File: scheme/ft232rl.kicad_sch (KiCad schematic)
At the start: 10 parts, among them J3 USB_B_Mini, U3 FT232RL

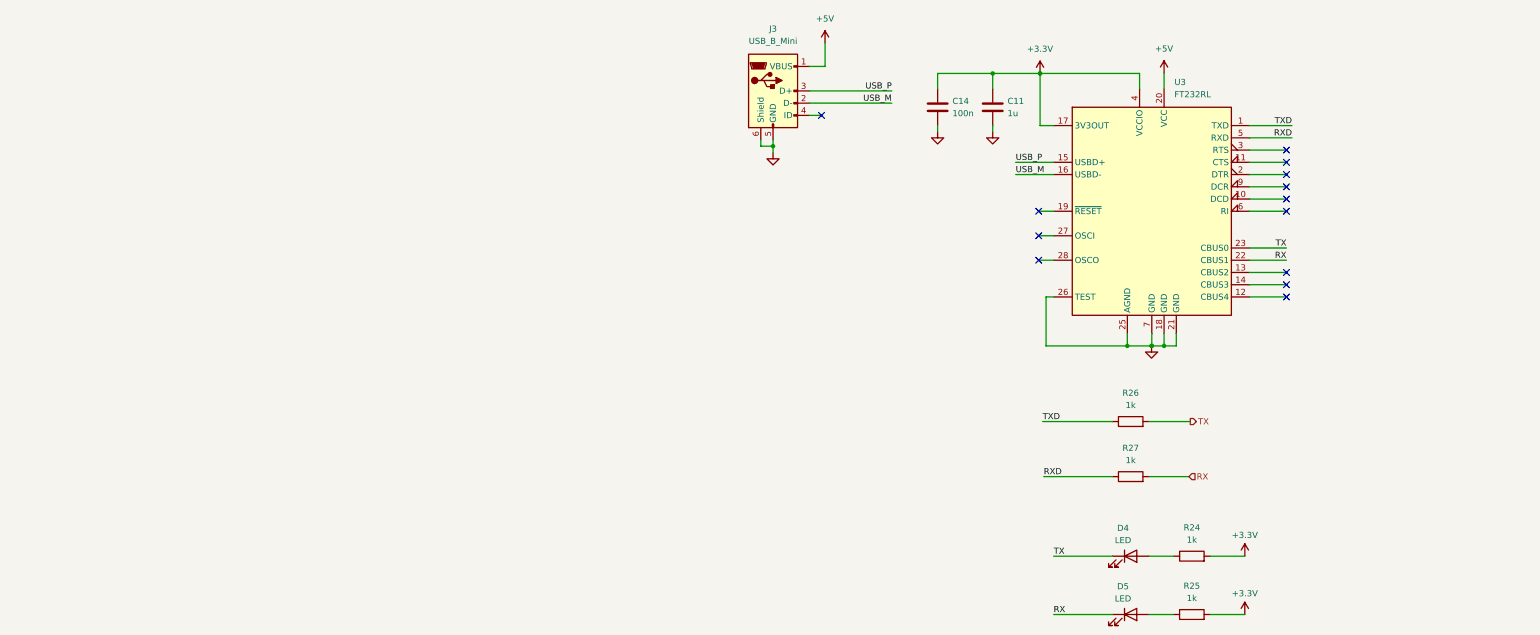
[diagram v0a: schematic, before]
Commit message: feat(schematic): fix peripheral sheets and integrate STM32G0B1CCT6
Главный МК заменён на STM32G0B1CCT6 (LQFP-48, pin-to-pin совместим
с STM32G071CBT6). Лист cpu переписан: обвязка по DS13560, LSE
32.768 кГц, подстроечник на ADC (PA4), перемычка JP_IDD, таблица
назначения выводов.

Исправлены листы периферии:
- st_link: перепутанные USB D+/D-, закороченные резисторы SWD,
  VBUS через PTC и Шоттки, ESD USBLC6-2SC6, LDO AP7361C-33E,
  SWO стянут на землю, J2 1x5 с NRST, перемычка JP_STL_PWR;
- ft232rl: 3V3OUT отвязан от общей шины +3.3V, разделены цепи
  TX/RX и светодиодов, ESD, Шоттки на VBUS, делитель на RESET#;
- w5500: номиналы терминации MDI (49.9 Ом / 10 Ом), PMODE=111,
  RSVD на GND, бусина аналогового питания, подтяжки RST/SCS/INT;
- w32: флэш W25Q32JVSSIQ, символ microSD с детектом карты,
  подтяжки линий SD;
- tmp10x: подтяжки I2C, адреса без резисторов, развязка 100 нФ.

Добавлен лист headers: разъёмы Arduino Uno R3 без ICSP, гребёнки
логического анализатора 1x27 с двух сторон, перемычки JP_SWD.
Удалён пустой лист memory. ERC: 0 ошибок.
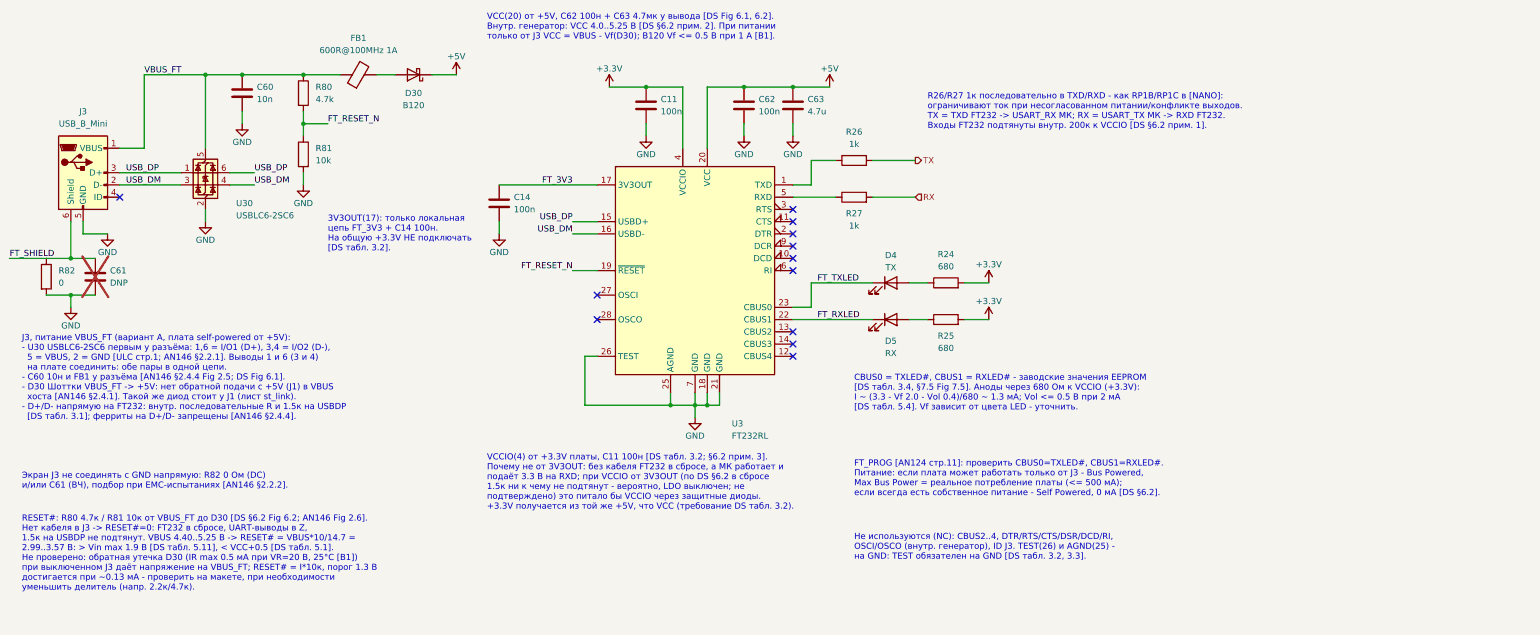
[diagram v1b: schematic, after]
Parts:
- added C60: 10n, Capacitor_SMD:C_0805_2012Metric, symbol Device:C
- added C61: DNP, Capacitor_SMD:C_0805_2012Metric, symbol Device:C
- added C62: 100n, Capacitor_SMD:C_0805_2012Metric, symbol Device:C
- added C63: 4.7u, Capacitor_SMD:C_0805_2012Metric, symbol Device:C
- added D30: B120, Diode_SMD:D_SMA, symbol Device:D_Schottky
- added FB1: 600R@100MHz 1A, Inductor_SMD:L_0805_2012Metric, symbol Device:FerriteBead
- added R80: 4.7k, Resistor_SMD:R_0805_2012Metric, symbol Device:R
- added R81: 10k, Resistor_SMD:R_0805_2012Metric, symbol Device:R
- added R82: 0, Resistor_SMD:R_0805_2012Metric, symbol Device:R
- added U30: USBLC6-2SC6, Package_TO_SOT_SMD:SOT-23-6, symbol Power_Protection:USBLC6-2SC6
- C11: value 1u -> 100n; footprint (none) -> Capacitor_SMD:C_0805_2012Metric
- C14: footprint (none) -> Capacitor_SMD:C_0805_2012Metric
- D4: value LED -> TX; footprint (none) -> LED_SMD:LED_0805_2012Metric
- D5: value LED -> RX; footprint (none) -> LED_SMD:LED_0805_2012Metric
- R24, R25: value 1k -> 680; footprint (none) -> Resistor_SMD:R_0805_2012Metric
- R26, R27: footprint (none) -> Resistor_SMD:R_0805_2012Metric
- U3: FT_PROG (none) -> CBUS0=TXLED#, CBUS1=RXLED#, Power: Bus Powered + Max Bus Po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
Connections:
- net +3.3V: no longer C14.1, U3.17 (3V3OUT)
- net +5V: now also C62.1, C63.1, D30.1 (K); no longer J3.1 (VBUS)
- net GND: now also C60.2, C61.2, C62.2, C63.2, R81.2, R82.2, U30.2 (GND); no longer J3.6 (Shield)
- net RX: no longer D5.1 (K), U3.22 (CBUS1)
- net TX: no longer D4.1 (K), U3.23 (CBUS0)
- net FT_RESET_N: now reaches U3.19 (~{RESET})
- net FT_RESET_N: now also R80.2, R81.1
- net RXD: no longer names the net of R27.1, U3.5 (RXD)
- net TXD: no longer names the net of R26.1, U3.1 (TXD)
- net USB_M renamed USB_DM
- net USB_DM: now also U30.3 (I/O2), U30.4 (I/O2)
- net USB_P renamed USB_DP
- net USB_DP: now also U30.1 (I/O1), U30.6 (I/O1)
- new net: D30.2 (A), FB1.2
- new net FT_3V3: C14.1, U3.17 (3V3OUT)
- new net FT_RXLED: D5.1 (K), U3.22 (CBUS1)
- new net FT_SHIELD: C61.1, J3.6 (Shield), R82.1
- new net FT_TXLED: D4.1 (K), U3.23 (CBUS0)
- new net VBUS_FT: C60.1, FB1.1, J3.1 (VBUS), R80.1, U30.5 (VBUS)
- no-connect marks 13 -> 12
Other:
- note added: "3V3OUT(17): только локальная цепь FT_3V3 + C14 100н. На общую +3.3V НЕ подключать [DS табл. 3.2]."
- note added: "CBUS0 = TXLED#, CBUS1 = RXLED# - заводские значения EEPROM [DS табл. 3.4, §7.5 Fig 7.5]. Аноды через 680 Ом к VCCIO (+3.3V): I ~ (3.3 - Vf 2.0 - Vol 0.4)/680 ~ 1.3 мА; Vol <= 0.5 В при 2 мА [DS табл. 5.4]. Vf зависит от цвета LED - уточнить."
- note added: "FT_PROG [AN124 стр.11]: проверить CBUS0=TXLED#, CBUS1=RXLED#. Питание: если плата может работать только от J3 - Bus Powered, Max Bus Power = реальное потребление платы (<= 500 мА); если всегда есть собственное питание - Self Powered, 0 мА [DS §6.2]."
- note added: "J3, питание VBUS_FT (вариант A, плата self-powered от +5V): - U30 USBLC6-2SC6 первым у разъёма: 1,6 = I/O1 (D+), 3,4 = I/O2 (D-), 5 = VBUS, 2 = GND [ULC стр.1; AN146 §2.2.1]. Выводы 1 и 6 (3 и 4) на плате соединить: обе пары в одной цепи. - C60 10н и FB1 у разъёма [AN146 §2.4.4 Fig 2.5; DS Fig 6.1]. - D30 Шоттки VBUS_FT -> +5V: нет обратной подачи с +5V (J1) в VBUS хоста [AN146 §2.4.1]. Такой же 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"
- note added: "R26/R27 1к последовательно в TXD/RXD - как RP1B/RP1C в [NANO]: ограничивают ток при несогласованном питании/конфликте выходов. TX = TXD FT232 -> USART_RX МК; RX = USART_TX МК -> RXD FT232. Входы FT232 подтянуты внутр. 200к к VCCIO [DS §6.2 прим. 1]."
- note added: "RESET#: R80 4.7к / R81 10к от VBUS_FT до D30 [DS §6.2 Fig 6.2; AN146 Fig 2.6]. Нет кабеля в J3 -> RESET#=0: FT232 в сбросе, UART-выводы в Z, 1.5к на USBDP не подтянут. VBUS 4.40..5.25 В -> RESET# = VBUS*10/14.7 = 2.99..3.57 В: > Vin max 1.9 В [DS табл. 5.11], < VCC+0.5 [DS табл. 5.1]. Не проверено: обратная утечка D30 (IR max 0.5 мА при VR=20 В, 25°C [B1]) при выключенном J3 даёт напряжение на VB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"
- note added: "VCC(20) от +5V, C62 100н + C63 4.7мк у вывода [DS Fig 6.1, 6.2]. Внутр. генератор: VCC 4.0..5.25 В [DS §6.2 прим. 2]. При питании только от J3 VCC = VBUS - Vf(D30); B120 Vf <= 0.5 В при 1 А [B1]."
- note added: "VCCIO(4) от +3.3V платы, C11 100н [DS табл. 3.2; §6.2 прим. 3]. Почему не от 3V3OUT: без кабеля FT232 в сбросе, а МК работает и подаёт 3.3 В на RXD; при VCCIO от 3V3OUT (по DS §6.2 в сбросе 1.5к ни к чему не подтянут - вероятно, LDO выключен; не подтверждено) это питало бы VCCIO через защитные диоды. +3.3V получается из той же +5V, что VCC (требование DS табл. 3.2)."
- note added: "Не используются (NC): CBUS2..4, DTR/RTS/CTS/DSR/DCD/RI, OSCI/OSCO (внутр. генератор), ID J3. TEST(26) и AGND(25) - на GND: TEST обязателен на GND [DS табл. 3.2, 3.3]."
- note added: "Экран J3 не соединять с GND напрямую: R82 0 Ом (DC) и/или C61 (ВЧ), подбор при EMC-испытаниях [AN146 §2.2.2]."
- moved on the sheet: C11, C14, D4, D5, J3, R24, R25, R26, R27, U3

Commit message: refactor(schematic): re-annotate references by sheet number
Позиционные обозначения перенумерованы по схеме «номер листа x 100»:
cpu - 1xx, st_link - 2xx, ft232rl - 3xx, w5500 - 4xx, w32 - 5xx,
tmp10x - 6xx, leds - 7xx, headers - 8xx. По обозначению на плате
сразу видно, к какому листу относится компонент.

Ссылки на компоненты в текстовых комментариях обновлены. Обозначения
из сторонних референсных схем (MB1136, MB1184, W5500-Ref, Ethernet
Shield, Adafruit) и имена выводов Arduino оставлены без изменений.

Проверено: нетлист до и после совпадает с точностью до переименования
(190 цепей, 187 компонентов), дубликатов нет, ERC - 0 ошибок.
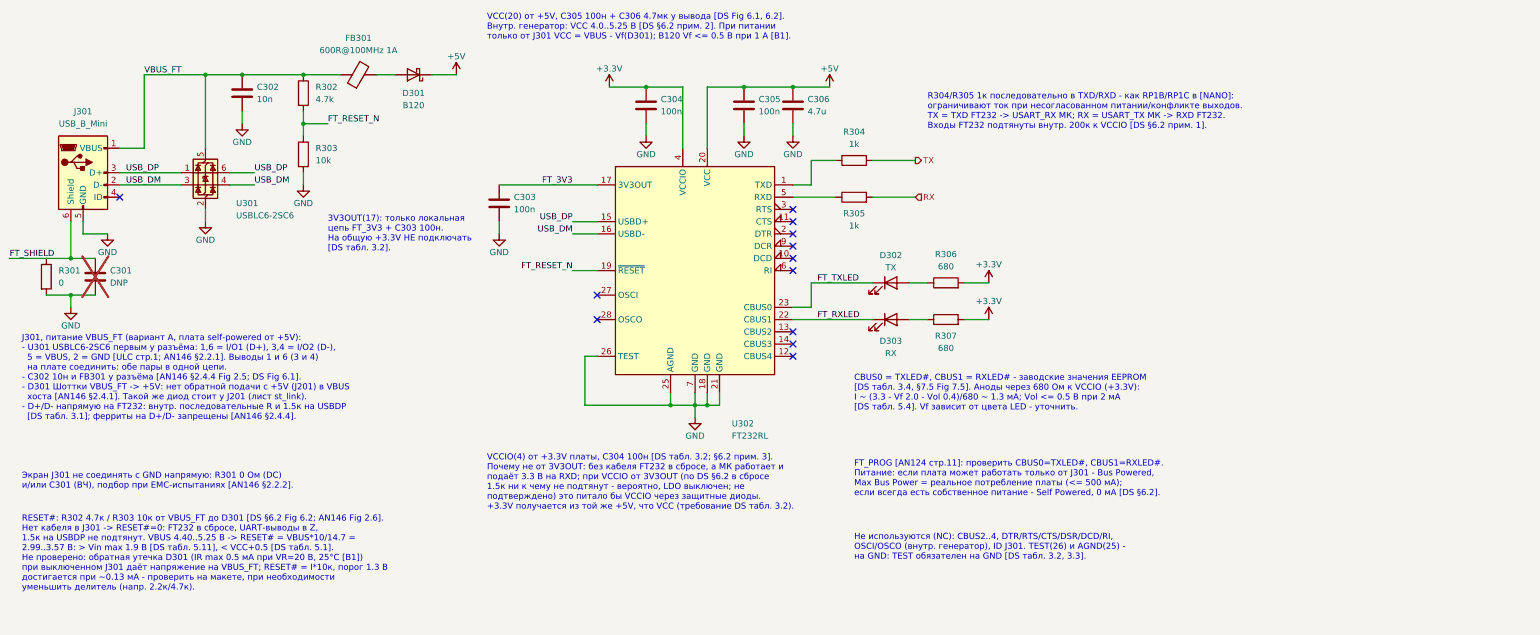
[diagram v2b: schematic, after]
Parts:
- renumbered C61 to C301, C60 to C302, C14 to C303, C11 to C304, C62 to C305, C63 to C306, D30 to D301, D4 to D302, D5 to D303, FB1 to FB301, J3 to J301, R82 to R301, R80 to R302, R81 to R303, R26 to R304, R27 to R305, R24 to R306, R25 to R307, U30 to U301, U3 to U302
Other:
- note added: "3V3OUT(17): только локальная цепь FT_3V3 + C303 100н. На общую +3.3V НЕ подключать [DS табл. 3.2]."
- note added: "FT_PROG [AN124 стр.11]: проверить CBUS0=TXLED#, CBUS1=RXLED#. Питание: если плата может работать только от J301 - Bus Powered, Max Bus Power = реальное потребление платы (<= 500 мА); если всегда есть собственное питание - Self Powered, 0 мА [DS §6.2]."
- note added: "J301, питание VBUS_FT (вариант A, плата self-powered от +5V): - U301 USBLC6-2SC6 первым у разъёма: 1,6 = I/O1 (D+), 3,4 = I/O2 (D-), 5 = VBUS, 2 = GND [ULC стр.1; AN146 §2.2.1]. Выводы 1 и 6 (3 и 4) на плате соединить: обе пары в одной цепи. - C302 10н и FB301 у разъёма [AN146 §2.4.4 Fig 2.5; DS Fig 6.1]. - D301 Шоттки VBUS_FT -> +5V: нет обратной подачи с +5V (J201) в VBUS хоста [AN146 §2.4.1]. 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"
- note added: "R304/R305 1к последовательно в TXD/RXD - как RP1B/RP1C в [NANO]: ограничивают ток при несогласованном питании/конфликте выходов. TX = TXD FT232 -> USART_RX МК; RX = USART_TX МК -> RXD FT232. Входы FT232 подтянуты внутр. 200к к VCCIO [DS §6.2 прим. 1]."
- note added: "RESET#: R302 4.7к / R303 10к от VBUS_FT до D301 [DS §6.2 Fig 6.2; AN146 Fig 2.6]. Нет кабеля в J301 -> RESET#=0: FT232 в сбросе, UART-выводы в Z, 1.5к на USBDP не подтянут. VBUS 4.40..5.25 В -> RESET# = VBUS*10/14.7 = 2.99..3.57 В: > Vin max 1.9 В [DS табл. 5.11], < VCC+0.5 [DS табл. 5.1]. Не проверено: обратная утечка D301 (IR max 0.5 мА при VR=20 В, 25°C [B1]) при выключенном J301 даёт напряжен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"
- note added: "VCC(20) от +5V, C305 100н + C306 4.7мк у вывода [DS Fig 6.1, 6.2]. Внутр. генератор: VCC 4.0..5.25 В [DS §6.2 прим. 2]. При питании только от J301 VCC = VBUS - Vf(D301); B120 Vf <= 0.5 В при 1 А [B1]."
- note added: "VCCIO(4) от +3.3V платы, C304 100н [DS табл. 3.2; §6.2 прим. 3]. Почему не от 3V3OUT: без кабеля FT232 в сбросе, а МК работает и подаёт 3.3 В на RXD; при VCCIO от 3V3OUT (по DS §6.2 в сбросе 1.5к ни к чему не подтянут - вероятно, LDO выключен; не подтверждено) это питало бы VCCIO через защитные диоды. +3.3V получается из той же +5V, что VCC (требование DS табл. 3.2)."
- note added: "Не используются (NC): CBUS2..4, DTR/RTS/CTS/DSR/DCD/RI, OSCI/OSCO (внутр. генератор), ID J301. TEST(26) и AGND(25) - на GND: TEST обязателен на GND [DS табл. 3.2, 3.3]."
- note added: "Экран J301 не соединять с GND напрямую: R301 0 Ом (DC) и/или C301 (ВЧ), подбор при EMC-испытаниях [AN146 §2.2.2]."
- note removed: "3V3OUT(17): только локальная цепь FT_3V3 + C14 100н. На общую +3.3V НЕ подключать [DS табл. 3.2]."
- note removed: "FT_PROG [AN124 стр.11]: проверить CBUS0=TXLED#, CBUS1=RXLED#. Питание: если плата может работать только от J3 - Bus Powered, Max Bus Power = реальное потребление платы (<= 500 мА); если всегда есть собственное питание - Self Powered, 0 мА [DS §6.2]."
- note removed: "J3, питание VBUS_FT (вариант A, плата self-powered от +5V): - U30 USBLC6-2SC6 первым у разъёма: 1,6 = I/O1 (D+), 3,4 = I/O2 (D-), 5 = VBUS, 2 = GND [ULC стр.1; AN146 §2.2.1]. Выводы 1 и 6 (3 и 4) на плате соединить: обе пары в одной цепи. - C60 10н и FB1 у разъёма [AN146 §2.4.4 Fig 2.5; DS Fig 6.1]. - D30 Шоттки VBUS_FT -> +5V: нет обратной подачи с +5V (J1) в VBUS хоста [AN146 §2.4.1]. Такой же 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"
- note removed: "R26/R27 1к последовательно в TXD/RXD - как RP1B/RP1C в [NANO]: ограничивают ток при несогласованном питании/конфликте выходов. TX = TXD FT232 -> USART_RX МК; RX = USART_TX МК -> RXD FT232. Входы FT232 подтянуты внутр. 200к к VCCIO [DS §6.2 прим. 1]."
- note removed: "RESET#: R80 4.7к / R81 10к от VBUS_FT до D30 [DS §6.2 Fig 6.2; AN146 Fig 2.6]. Нет кабеля в J3 -> RESET#=0: FT232 в сбросе, UART-выводы в Z, 1.5к на USBDP не подтянут. VBUS 4.40..5.25 В -> RESET# = VBUS*10/14.7 = 2.99..3.57 В: > Vin max 1.9 В [DS табл. 5.11], < VCC+0.5 [DS табл. 5.1]. Не проверено: обратная утечка D30 (IR max 0.5 мА при VR=20 В, 25°C [B1]) при выключенном J3 даёт напряжение на VB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"
- note removed: "VCC(20) от +5V, C62 100н + C63 4.7мк у вывода [DS Fig 6.1, 6.2]. Внутр. генератор: VCC 4.0..5.25 В [DS §6.2 прим. 2]. При питании только от J3 VCC = VBUS - Vf(D30); B120 Vf <= 0.5 В при 1 А [B1]."
- note removed: "VCCIO(4) от +3.3V платы, C11 100н [DS табл. 3.2; §6.2 прим. 3]. Почему не от 3V3OUT: без кабеля FT232 в сбросе, а МК работает и подаёт 3.3 В на RXD; при VCCIO от 3V3OUT (по DS §6.2 в сбросе 1.5к ни к чему не подтянут - вероятно, LDO выключен; не подтверждено) это питало бы VCCIO через защитные диоды. +3.3V получается из той же +5V, что VCC (требование DS табл. 3.2)."
- note removed: "Не используются (NC): CBUS2..4, DTR/RTS/CTS/DSR/DCD/RI, OSCI/OSCO (внутр. генератор), ID J3. TEST(26) и AGND(25) - на GND: TEST обязателен на GND [DS табл. 3.2, 3.3]."
- note removed: "Экран J3 не соединять с GND напрямую: R82 0 Ом (DC) и/или C61 (ВЧ), подбор при EMC-испытаниях [AN146 §2.2.2]."

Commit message: fix(schematic): resolve all ERC warnings
ERC: 0 ошибок, 0 предупреждений (было 239 предупреждений).

- w5500, leds: все объекты перенесены на сетку 1.27 мм; удалены
  два провода нулевой длины.
- Заведена проектная библиотека g0_dev_board.kicad_sym (+ sym-lib-table)
  для намеренно изменённых символов: USB_B_Mini с пассивными
  VBUS/GND (J201, J301). Попутно исправлен номер вывода экрана
  6 -> SH: у footprint Lumberg 2486 01 площадки экрана называются SH,
  иначе экран на плате остался бы неподключённым.
- Устаревшие копии символа LED обновлены из стандартной библиотеки.
- Кнопки SW701/SW702: SW_DPST_x2 заменён на SW_Push, footprint
  SW_SPST_PTS645Sx43SMTR92 (площадки 1,1,2,2 уже попарно замкнуты).
- Флэш U501: WP и HOLD подтянуты к +3.3V через R516/R517 10k
  вместо прямого подключения к выходу LDO.

Связность проверена сравнением нетлистов: изменились только цепи
WP/HOLD флэша.
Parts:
- J301: symbol Connector:USB_B_Mini -> g0_dev_board:USB_B_Mini
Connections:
- net FT_SHIELD: now also J301.SH (Shield); no longer J301.6 (Shield)
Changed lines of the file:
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@@
 	)
 	(symbol
-		(lib_id "Connector:USB_B_Mini")
+		(lib_id "g0_dev_board:USB_B_Mini")
 		(at 30.48 50.8 0)
 		(unit 1)
@@
 		(pin "5"
 		)
-		(pin "6"
+		(pin "SH"
 		)
 		(instances

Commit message: fix(schematic): harden FT232 reset and reduce NRST load
- FT232RL: делитель RESET# R302/R303 4.7k/10k -> 1k/2.2k. Обратная
  утечка Шоттки D301 при питании платы от ST-Link поднимала RESET#
  к порогу; теперь порог достигается при 0.59 мА, что выше
  гарантированного IR max B120.
- ST-Link: PTC F201 MF-MSMF050 -> MF-MSMF075 (R1max 1.0 -> 0.45 Ом),
  чтобы VCC FT232 оставался >= 4.0 В в худшем случае.
- NRST: C701 и R703 на листе leds -> DNP. Остаются C103 100n у вывода
  и внутренняя подтяжка, как рекомендует ST (DS13560 рис. 27) и как на
  NUCLEO MB1136.
- SW702: значение RESET -> USER (это пользовательская кнопка на PC13).

Комментарии на схеме обновлены. ERC: 0 ошибок, 0 предупреждений.
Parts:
- R302: value 4.7k -> 1k
- R303: value 10k -> 2.2k
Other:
- note added: "RESET#: R302 1к / R303 2.2к от VBUS_FT до D301 [DS §6.2 Fig 6.2; AN146 Fig 2.6]. Нет кабеля в J301 -> RESET#=0: FT232 в сбросе, UART-выводы в Z, 1.5к на USBDP не подтянут. VBUS 4.40..5.25 В -> RESET# = VBUS*2.2/3.2 = 3.03..3.61 В: > Vin max 1.9 В [DS табл. 5.11], < VCC+0.5 [DS табл. 5.1]. Делитель уменьшен с 4.7к/10к: обратная утечка D301 B120 при питании платы от J201 течёт в VBUS_FT и через R30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"
- note removed: "RESET#: R302 4.7к / R303 10к от VBUS_FT до D301 [DS §6.2 Fig 6.2; AN146 Fig 2.6]. Нет кабеля в J301 -> RESET#=0: FT232 в сбросе, UART-выводы в Z, 1.5к на USBDP не подтянут. VBUS 4.40..5.25 В -> RESET# = VBUS*10/14.7 = 2.99..3.57 В: > Vin max 1.9 В [DS табл. 5.11], < VCC+0.5 [DS табл. 5.1]. Не проверено: обратная утечка D301 (IR max 0.5 мА при VR=20 В, 25°C [B1]) при выключенном J301 даёт напряжен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"
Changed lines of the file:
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@@
 		(date "2026-07-04")
 	)
-	(text "RESET#: R302 4.7к / R303 10к от VBUS_FT до D301 [DS §6.2 Fig 6.2; AN146 Fig 2.6].\nНет кабеля в J301 -> RESET#=0: FT232 в сбросе, UART-выводы в Z,\n1.5к на USBDP не подтянут. VBUS 4.40..5.25 В -> RESET# = VBUS*10/14.7 =\n2.99..3.57 В: > Vin max 1.9 В [DS табл. 5.11], < VCC+0.5 [DS табл. 5.1].\nНе проверено: обратная утечка D301 (IR max 0.5 мА при VR=20 В, 25°C [B1])\nпри выключенном J301 даёт напряжение на VBUS_FT; RESET# = I*10к, порог 1.3 В\nдостигается при ~0.13 мА - проверить на макете, при необходимости\nуменьшить делитель (напр. 2.2к/4.7к)."
+	(text "RESET#: R302 1к / R303 2.2к от VBUS_FT до D301 [DS §6.2 Fig 6.2; AN146 Fig 2.6].\nНет кабеля в J301 -> RESET#=0: FT232 в сбросе, UART-выводы в Z,\n1.5к на USBDP не подтянут. VBUS 4.40..5.25 В -> RESET# = VBUS*2.2/3.2 =\n3.03..3.61 В: > Vin max 1.9 В [DS табл. 5.11], < VCC+0.5 [DS табл. 5.1].\nДелитель уменьшен с 4.7к/10к: обратная утечка D301 B120 при питании платы от J201\nтечёт в VBUS_FT и через R303 поднимает RESET#. Порог 1.3 В теперь при I = 0.59 мА,\nчто выше гарантированного IR max 0.5 мА (VR=20 В, 25°C [B1]); при 85°C запас ~6.5x\nк типовой утечке (Fig.3 [B1], экстраполяция на 5 В). Ток с VBUS 1.6 мА."
 		(exclude_from_sim no)
 		(at 17.78 121.92 0)
@@
 			)
 		)
-		(property "Value" "4.7k"
+		(property "Value" "1k"
 			(at 78.74 35.56 0)
 			(show_name no)
@@
 			)
 		)
-		(property "Value" "10k"
+		(property "Value" "2.2k"
 			(at 78.74 48.26 0)
 			(show_name no)
